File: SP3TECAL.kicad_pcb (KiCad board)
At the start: 2 copper layers, 50 x 50 mm, 15 parts, among them IC1 MM5230-03NDB-TR, IC2 MM5230-03NDB-TR, IC3 MM5230-03NDB-TR, IC4 MM5230-03NDB-TR, J1 Conn_Coaxial, J2 Conn_Coaxial, J3 Conn_Coaxial, J4 Conn_Coaxial, J5 Conn_01x04, J6 Conn_01x04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

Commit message: much progress on routing
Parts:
- added R4: 56k, Resistor_SMD:R_0402_1005Metric, F.Cu at (171.6, 125.9)
- added R5: 56k, Resistor_SMD:R_0402_1005Metric, F.Cu at (174.9, 129.2)
- added R6: 56k, Resistor_SMD:R_0402_1005Metric, F.Cu at (179.2, 125.9)
- added REF**: MountingHole_3.2mm_M3, MountingHole:MountingHole_3.2mm_M3, F.Cu at (195.7, 112.7)
- added REF**: MountingHole_3.2mm_M3, MountingHole:MountingHole_3.2mm_M3, F.Cu at (195.7, 138.1)
- added REF**: MountingHole_3.2mm_M3, MountingHole:MountingHole_3.2mm_M3, F.Cu at (155.1, 138.1)
- added REF**: MountingHole_3.2mm_M3, MountingHole:MountingHole_3.2mm_M3, F.Cu at (155.1, 112.7)
- moved R3 61.5 mm to (167.8, 129.5), turned to 90 degrees
- moved J4 59.1 mm to (195.6, 125.4)
- moved IC4 57.6 mm to (167.8, 125.4)
- moved J2 57.5 mm to (154.9, 125.4)
- moved J5 57.4 mm to (198.9, 148.9)
- moved IC1 57.3 mm to (175.4, 125.4)
- moved IC3 57.3 mm to (175.4, 133.0)
- moved J6 57.2 mm to (191.3, 101.9)
- moved IC2 57.2 mm to (183.0, 125.4)
- moved J8 56.8 mm to (164.6, 148.9)
- moved J1 55.9 mm to (175.4, 105.1)
- moved J3 55.6 mm to (175.4, 145.6)
- moved R2 54.1 mm to (171.2, 133.0), turned to 180 degrees
- moved J7 54.0 mm to (151.9, 101.9), turned to 90 degrees
- moved R1 52.8 mm to (183.0, 129.5), turned to -90 degrees
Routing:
- net Net-(IC2-RF3GATE): track 0.00 -> 31.5 mm
- net Net-(IC2-RF2GATE): track 0.00 -> 30.7 mm
- net Net-(IC1-RF3GATE): track 0.00 -> 30.7 mm
- net Net-(IC1-RF1GATE): track 0.00 -> 30.2 mm
- net Net-(IC2-RF1GATE): track 0.00 -> 30.0 mm
- net Net-(IC4-RF4GATE): track 0.00 -> 29.6 mm
- net Net-(IC4-RF3GATE): track 0.00 -> 29.6 mm
- net Net-(IC1-RF2GATE): track 0.00 -> 29.4 mm
- net Net-(IC4-RF1GATE): track 0.00 -> 29.0 mm
- net Net-(IC1-RF4GATE): track 0.00 -> 28.9 mm
- net Net-(IC4-RF2GATE): track 0.00 -> 28.3 mm
- net Net-(IC3-RF4GATE): track 0.00 -> 28.2 mm
- net Net-(IC2-RF4GATE): track 0.00 -> 27.9 mm
- net Net-(IC3-RF3GATE): track 0.00 -> 26.8 mm
- net Net-(IC3-RF1GATE): track 0.00 -> 24.3 mm
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- added copper zone on B.Cu, net GND
- added copper zone on F.Cu, net GND
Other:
- board size 50 x 50 mm -> 50.8 x 50.8 mm

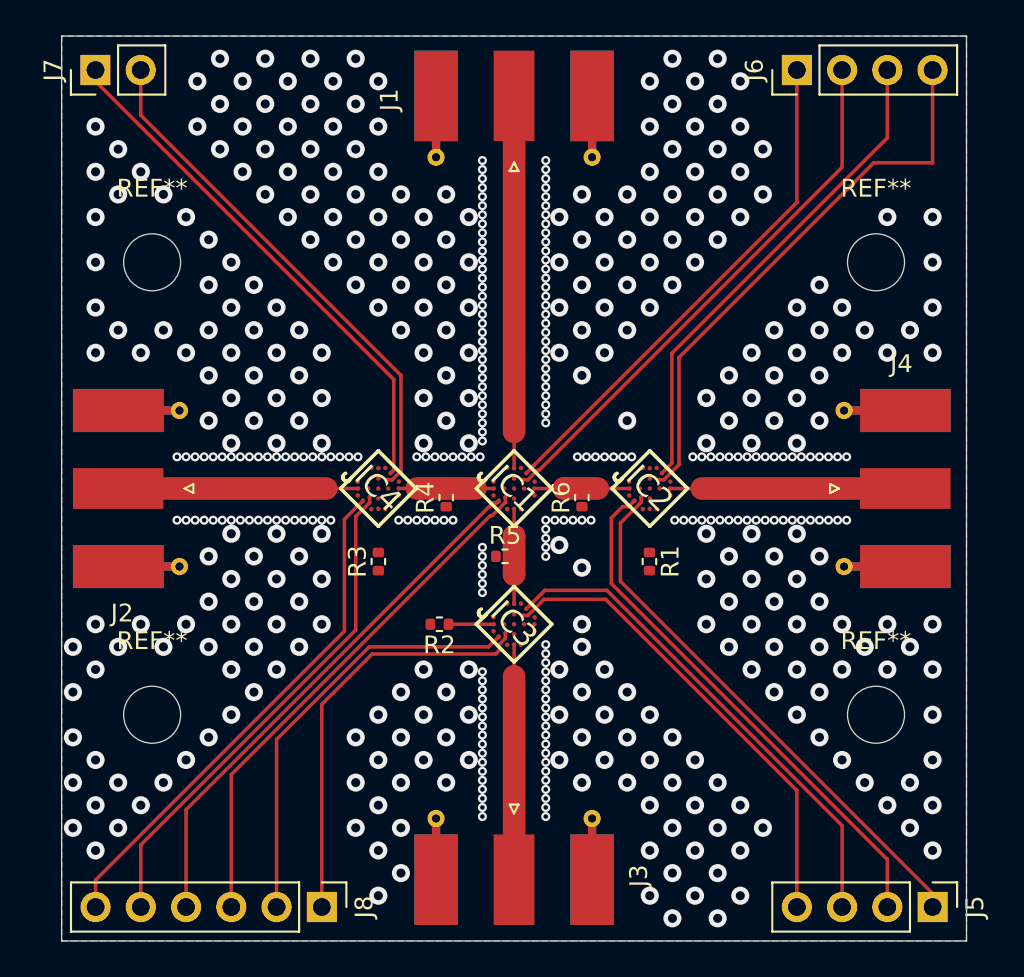
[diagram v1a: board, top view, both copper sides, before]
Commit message: adding SOL standards and switch as DUT board
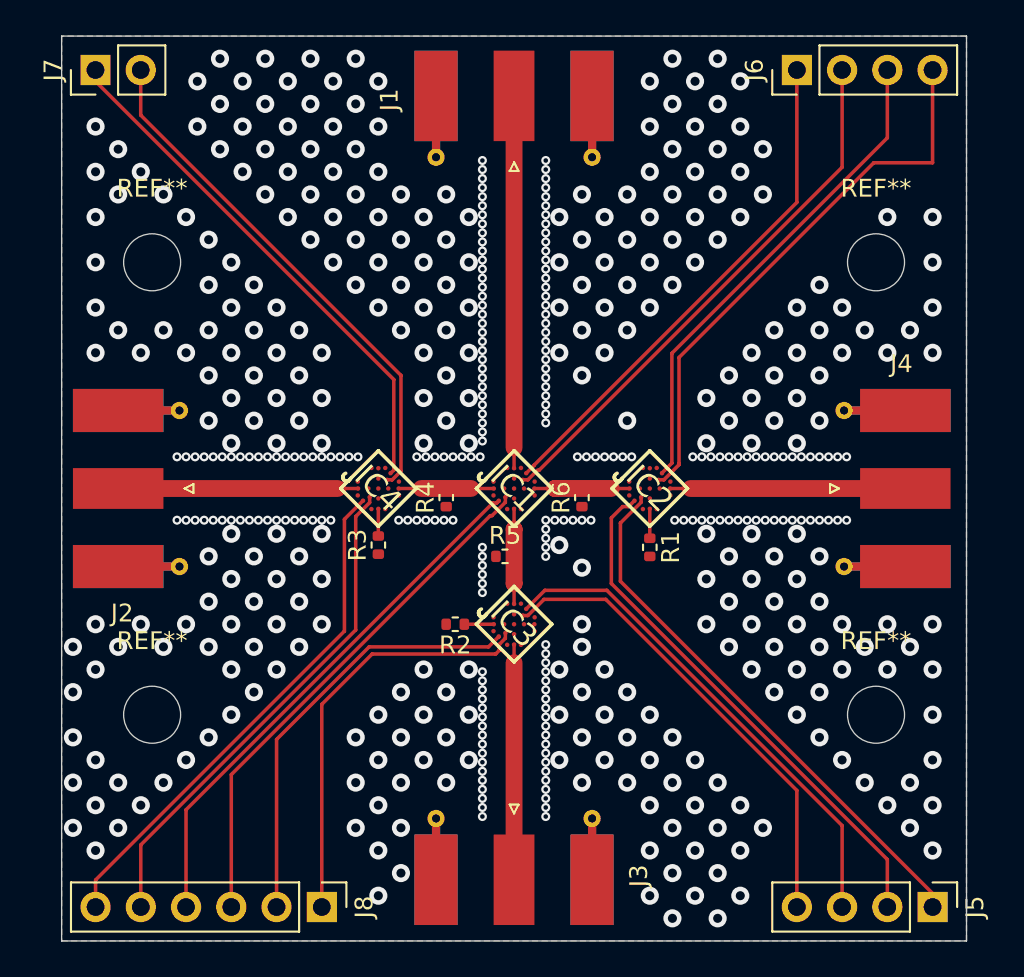
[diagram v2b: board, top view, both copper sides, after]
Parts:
- moved R3 0.93 mm to (167.8, 128.6)
- moved R2 0.89 mm to (172.1, 133.0)
- moved R1 0.80 mm to (183.0, 128.7)
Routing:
- net Net-(IC2-RF2): track 0.00 -> 1.65 mm
- net Net-(IC4-RF2): track 0.00 -> 1.53 mm
- net Net-(IC3-RF1): track 2.54 -> 1.65 mm
- net Net-(IC1-RF2): track 5.35 -> 6.24 mm

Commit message: updated SMA launch to SW microwave on all boards
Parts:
- J1, J2, J3, J4: footprint Connector_Coaxial:SMA_Molex_73251-1153_EdgeMount_Horizontal -> southwest-microwave-connectors:southwest-super-SMA-292-04A-12
- moved J3 5.31 mm to (175.4, 151.0)
- moved J1 5.23 mm to (175.4, 99.8)
- moved J4 5.18 mm to (200.8, 125.4)
- moved J2 4.90 mm to (150.0, 125.4)

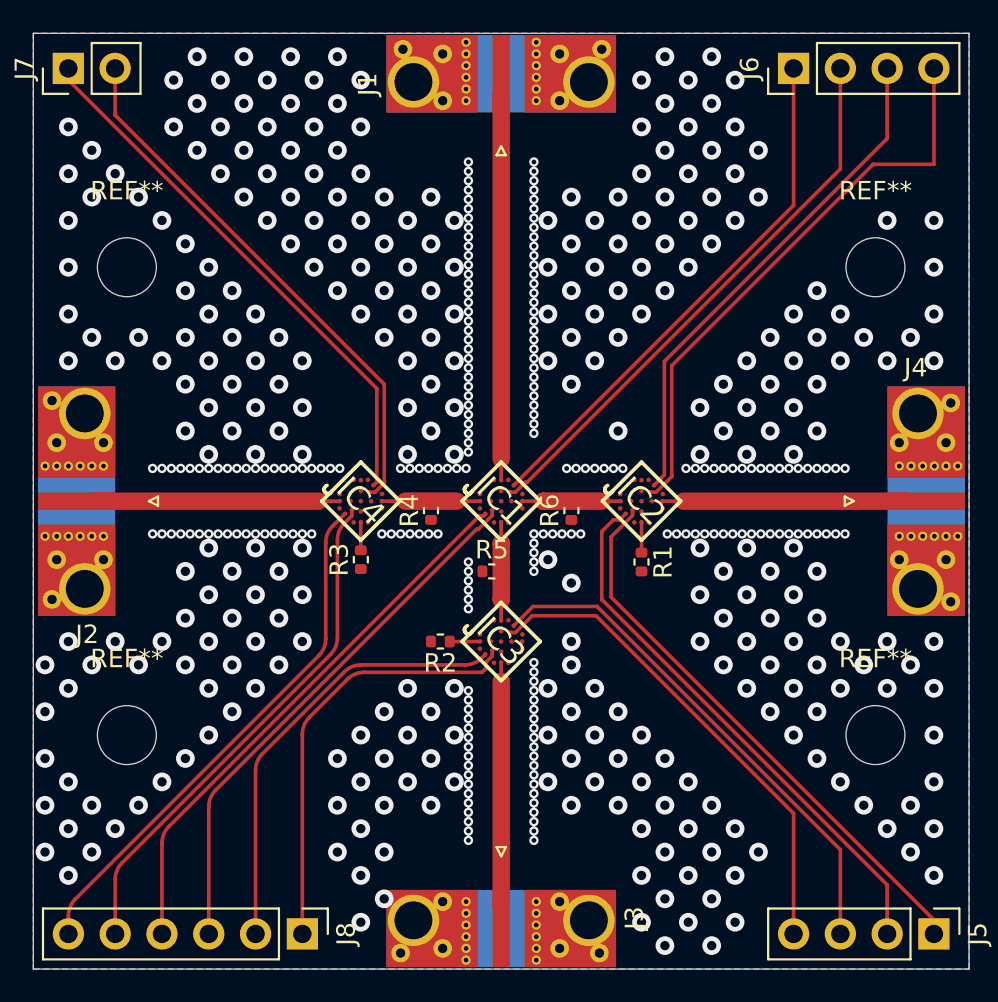
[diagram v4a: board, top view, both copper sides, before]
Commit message: used altium files to build kicad models of mm5800 and started new twpatron
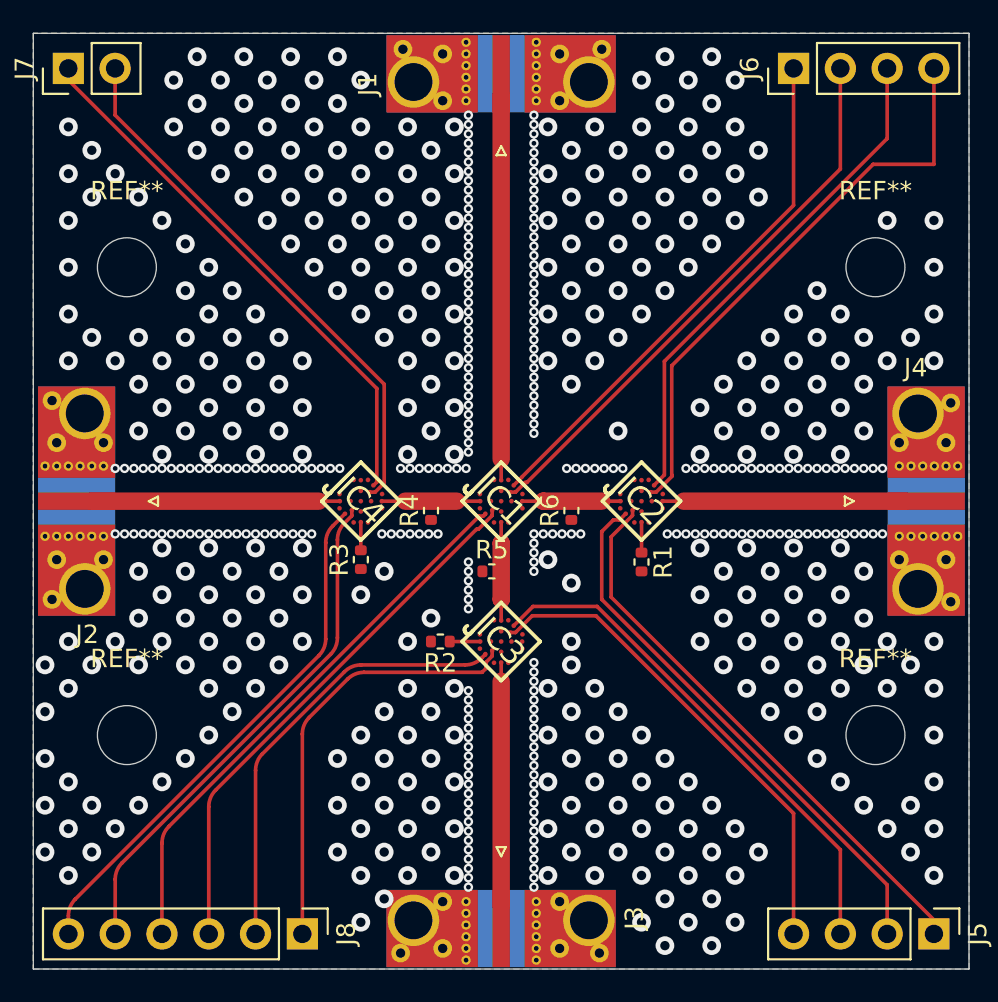
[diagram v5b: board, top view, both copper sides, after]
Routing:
- net GND: vias 530 -> 609
